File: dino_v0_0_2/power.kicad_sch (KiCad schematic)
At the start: 2 parts, among them J10 PS_ON, J9 ATX-24

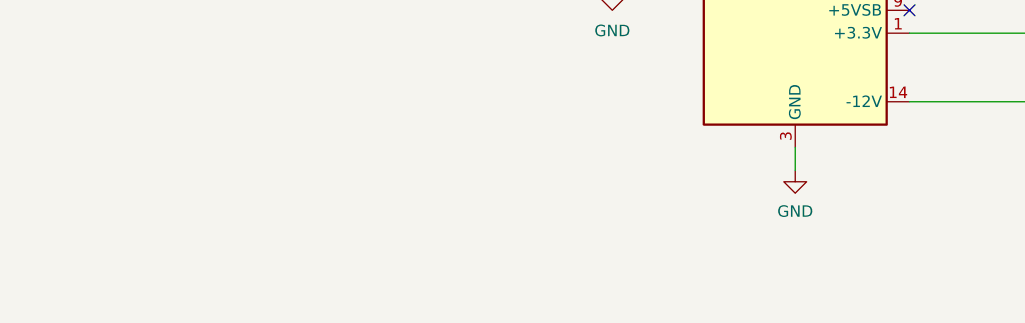
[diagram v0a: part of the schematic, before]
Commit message: feat(int): draw the interrupt block; sheet cleanup pass
New sheet dino_v0_0_2/interrupt.kicad_sch (page 15): U80-U87, R28 4.7k
pull-up on ~{IRQ}, R29 100R on the block's CLK branch, C83-C90. Every
pin per PHASE_INT SECTION 3, checked against the plan with kicad_netlist
and kicad-cli (146 pins, 0 mismatches).

Old sheets (SECTION 3.2): U28.4 lifted off GND to INJECT; U61.3 to
END_OR_ACCEPT; U36.1 to PC_UP_GATED; U49 D0-3 cut from U48 Za-Zd and
routed through U87 as FLAG_NEXT0-3 / FLAG_D0-3; FLAG_C/Z/V/N and the
five decoder outputs made global. dino_serial: U104 74LS05, INTR ->
~{IRQ}, C4.

Placement pass on every sheet: bus entries and global labels no longer
share wires; M, CW, T, IRB and SA buses kept as labelled keys. Nets
diffed against HEAD per sheet: only the intended changes and a rotated
C29. Project ERC: 0 errors. MODULE CONTRACT stamps regenerated.

Co-Authored-By: Claude Fable 5.1 <noreply@anthropic.com>
Claude-Session: https://claude.ai/code/session_01JGxSS4MVUcaZdKZGtKroSg
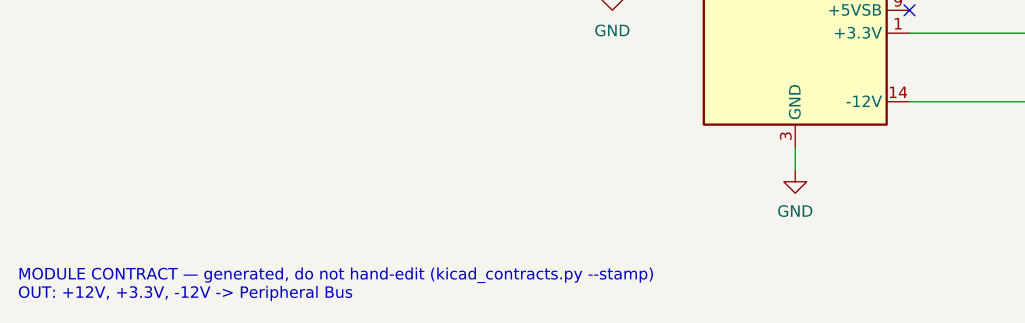
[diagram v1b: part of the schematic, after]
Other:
- note added: "MODULE CONTRACT — generated, do not hand-edit (kicad_contracts.py --stamp) OUT: +12V, +3.3V, -12V -> Peripheral Bus"
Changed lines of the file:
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@@
 		(comment 4 "A Turing-Complete 8-bit \"Computer\"")
+	)
+	(text "MODULE CONTRACT — generated, do not hand-edit (kicad_contracts.py --stamp)\nOUT: +12V, +3.3V, -12V -> Peripheral Bus"
+		(exclude_from_sim no)
+		(at 15.24 121.25 0)
+		(effects
+			(font
+				(size 1.27 1.27)
+			)
+			(justify left bottom)
+		)
 	)
 	(text "POWER IS OFF THE SHELF: picoPSU-160-XT or picoPSU-120-WI-25 in J9.\nRails drawn are what the unit delivers: +5V, +3.3V, +12V, -12V, GND.\nNo -5V exists on any 24-pin ATX unit since 2003; none is drawn.\n-12V is 50-100mA for the WHOLE machine (unit dependent): every card\nstates its +/-12V draw on its root page.\nPS_ON#: the unit runs while J10 is shorted. Panel switch or jumper.\n+5VSB and PWR_OK: real pins, nothing consumes them."

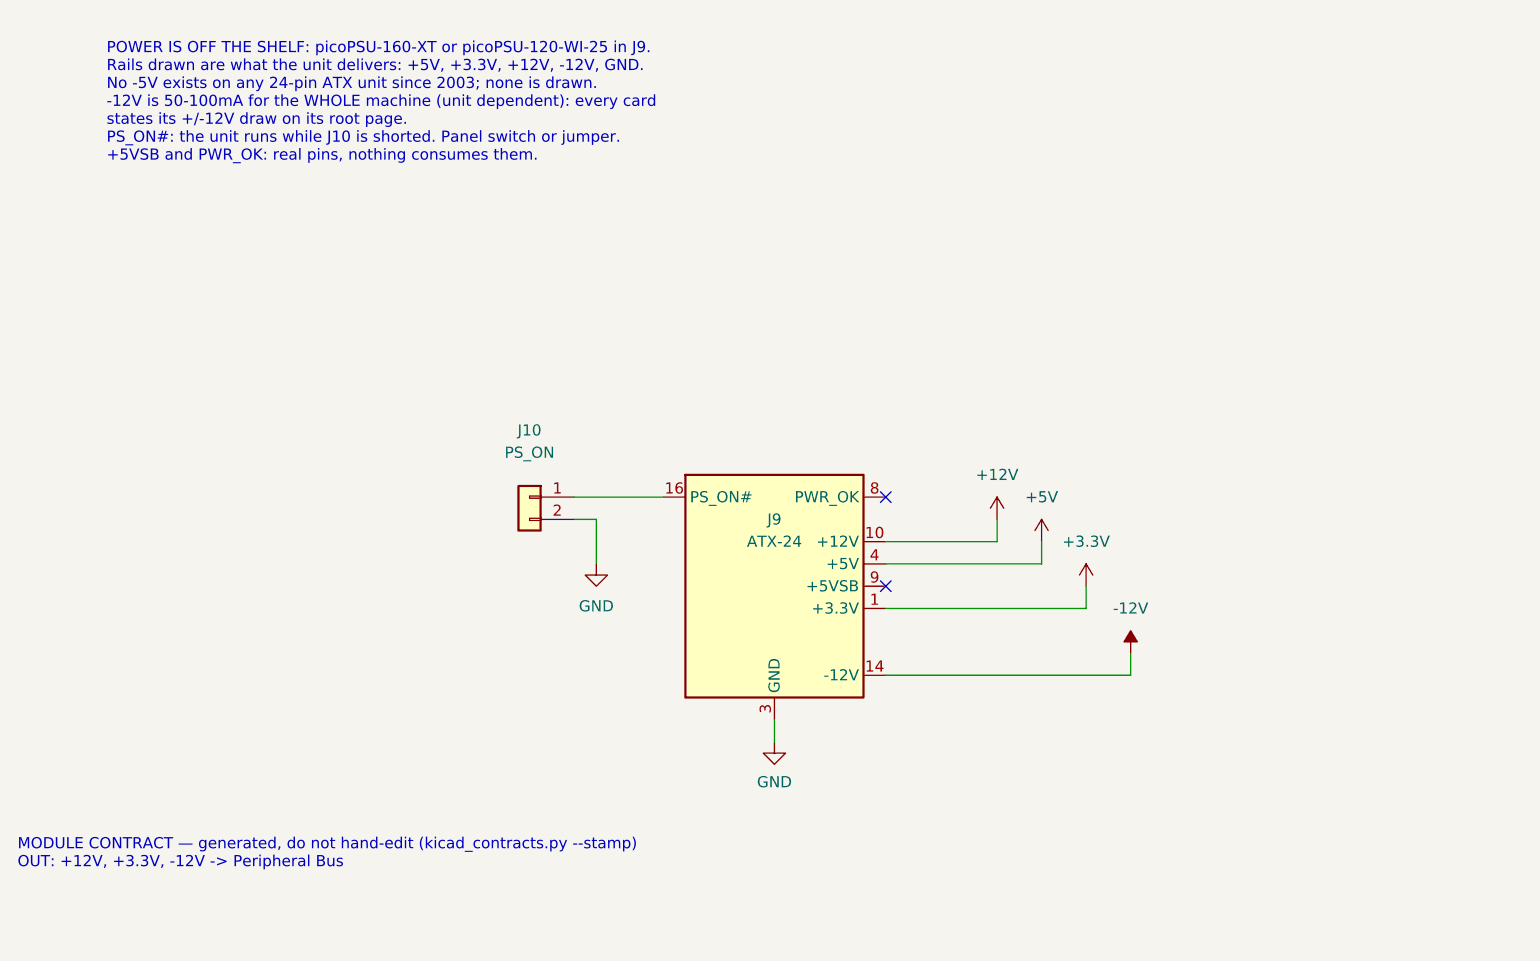
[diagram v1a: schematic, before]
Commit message: feat(pcb): sync board to schematic; fuse, bulk caps, RDY pull-up
Update PCB from schematic: the INT block (U80-U87), U76, the four
copper fixes (WR_GATE, CLK_ALU, INJECT, PC_UP gate) and the renumbered
W pull-ups (R9-R13, R30-R32 replace R4-R8, R25-R27). DRC schematic
parity 0.

Power: an old ATX tower supply into J9. +5V enters through F1 (3A
slow-blow, 5x20), J9's 5V pins on +5V_IN; C91 470uF + C92 10uF bulk;
PWR_FLAG on +5V. R33 10k pull-up on RDY. ERC unchanged from the
2026-10-06 baseline. Fix duplicate #PWR158 on the interrupt sheet.

Co-Authored-By: Claude Opus 5.5 <noreply@anthropic.com>
Claude-Session: https://claude.ai/code/session_01JGxSS4MVUcaZdKZGtKroSg
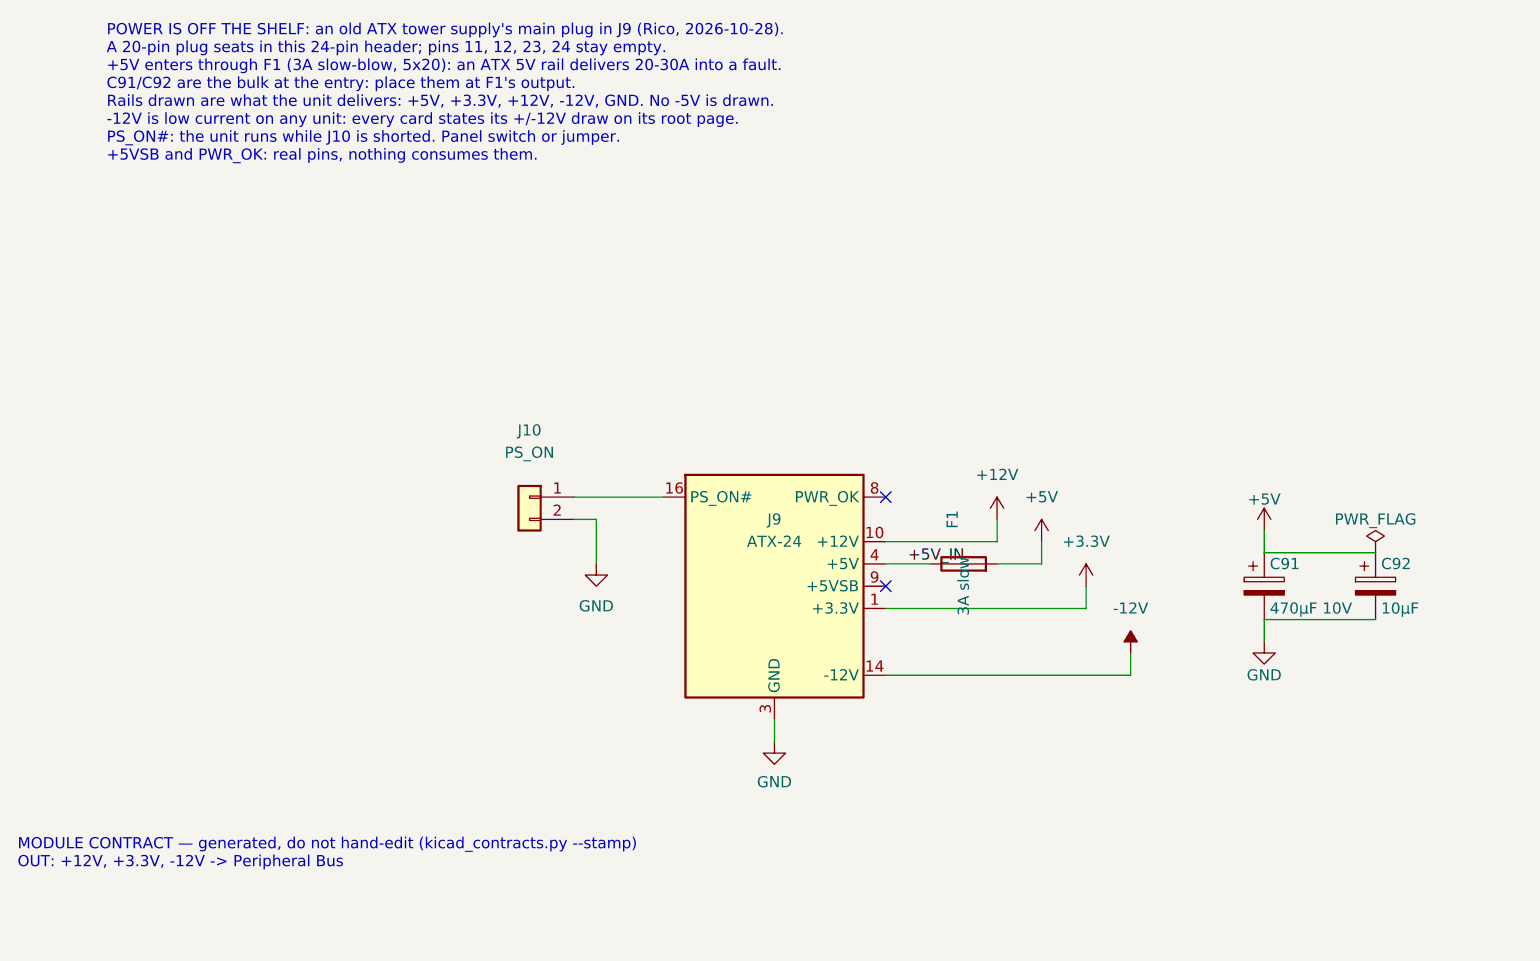
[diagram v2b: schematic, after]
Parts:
- added C91: 470µF 10V, Capacitor_THT:CP_Radial_D8.0mm_P3.50mm, symbol Device:C_Polarized
- added C92: 10µF, Capacitor_THT:CP_Radial_D5.0mm_P2.00mm, symbol Device:C_Polarized
- added F1: 3A slow, Fuse:Fuseholder_Cylinder-5x20mm_Schurter_0031_8201_Horizontal_Open, symbol Device:Fuse
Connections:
- net +5V: now also C91.1, C92.1, F1.2; no longer J9.21 (+5V), J9.22 (+5V), J9.23 (+5V), J9.4 (+5V), J9.6 (+5V)
- net GND: now also C91.2, C92.2
- new net +5V_IN: F1.1, J9.21 (+5V), J9.22 (+5V), J9.23 (+5V), J9.4 (+5V), J9.6 (+5V)
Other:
- note added: "POWER IS OFF THE SHELF: an old ATX tower supply's main plug in J9 (Rico, 2026-10-28). A 20-pin plug seats in this 24-pin header; pins 11, 12, 23, 24 stay empty. +5V enters through F1 (3A slow-blow, 5x20): an ATX 5V rail delivers 20-30A into a fault. C91/C92 are the bulk at the entry: place them at F1's output. Rails drawn are what the unit delivers: +5V, +3.3V, +12V, -12V, GND. No -5V is drawn. -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"
- note removed: "POWER IS OFF THE SHELF: picoPSU-160-XT or picoPSU-120-WI-25 in J9. Rails drawn are what the unit delivers: +5V, +3.3V, +12V, -12V, GND. No -5V exists on any 24-pin ATX unit since 2003; none is drawn. -12V is 50-100mA for the WHOLE machine (unit dependent): every card states its +/-12V draw on its root page. PS_ON#: the unit runs while J10 is shorted. Panel switch or jumper. +5VSB and PWR_OK: real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"

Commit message: feat(pcb): five grounded M3 mounting holes
H1-H5 (MountingHole_3.2mm_M3_Pad_Via, pad + stitching vias to the GND
plane) on the power sheet, pin 1 on GND. H1-H4 at the corners, 5 mm in
(H3 shifted to x 8.81 to clear J11); H5 at (85.88, 217.96), an interior
spot no track or part crosses, so the routing from 32aaa36 is unchanged.
KiCad DRC: 0 unconnected, 0 errors, 0 warnings, schematic parity 0.
ERC unchanged from the 2026-10-06 baseline.

Co-Authored-By: Claude Opus 5.5 <noreply@anthropic.com>
Claude-Session: https://claude.ai/code/session_01JGxSS4MVUcaZdKZGtKroSg
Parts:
- added H1, H2, H3, H4, H5: M3 GND, MountingHole:MountingHole_3.2mm_M3_Pad_Via, symbol Mechanical:MountingHole_Pad
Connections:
- net GND: now also H1.1, H2.1, H3.1, H4.1, H5.1

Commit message: feat(pcb): Rev 1.0 pre-order batch, debug access, no fuse
From the five-way pre-order review:

- Debug: J14 clock select at U27.3 (1.024 MHz / 512k / 256k / 128k /
  STEP), STEP debounced from SW3 through the spare U56 5->6 Schmitt;
  J15 LA header (16 control signals, a GND beside each); J16 power for
  the OB LEDs; DNP cap pads C94/C95/C96 on CLK at U6.2, CLK_ALU at
  U47.11 and CW15 (HALT) at U61.5; 15 GND scope loops so every IC but
  two is within 50 mm of one, plus a +5V test point.
- Power: F1 removed, no fuse (Rico); J9's +5V solid to the plane;
  bulk C97-C100 100 uF spread across the board; C92 ceramic.
- Layout: U6 beside U27 (its CLK pin was 138 mm out on raw CLK), C1/R1
  beside U56, RST_SIG in RESET and CLK_R / CLK_INT / CLK_M / CLK_SEL in
  CLK, thermal gap 0.3 mm (GND plane slots from 25 mm to under 8 mm),
  tracks >= 0.2 mm with no neckdown (6/6 mil tier), board min track rule.
- Values to match the bench: U56 SN7414N, U36 74LS00, U51 DM7400N,
  Y1 4.096 MHz.
- Edge socket: silk outline and a pin-1 arrow (unkeyed; a reversed card
  shorts +5V).

Re-routed by Freerouting 2.5.0 from an empty board. KiCad DRC 0
unconnected / 0 errors, schematic parity 0, one text_thickness warning
on the TrueType board text; ERC at its 74 baseline; test_pcb_envelope
7/7. Clock copper: CLK 296 mm, ~{CLK} 283, CLK_B 162, CLK_ALU 48.
Fab: fabrication/dino_rev_1_0_gerbers_20261029_1153.zip.

Co-Authored-By: Claude Opus 5.5 <noreply@anthropic.com>
Claude-Session: https://claude.ai/code/session_01JGxSS4MVUcaZdKZGtKroSg
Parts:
- removed F1: 3A slow, Fuse:Fuseholder_Cylinder-5x20mm_Schurter_0031_8201_Horizontal_Open, symbol Device:Fuse
- C92: value 10µF -> 10µF ceramic; footprint Capacitor_THT:CP_Radial_D5.0mm_P2.00mm -> Capacitor_THT:C_Disc_D5.0mm_W2.5mm_P2.50mm
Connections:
- net +5V_IN is gone; now on net +5V: J9.21 (+5V), J9.22 (+5V), J9.23 (+5V), J9.4 (+5V), J9.6 (+5V)
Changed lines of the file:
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@@
+		)
+	)
+	(wire
+		(pts
+			(xy 119.38 86.36)
+			(xy 127 86.36)
 		)
 	)
@@
 		)
 	)
-	(label "+5V_IN"
-		(at 116.84 86.36 0)
-		(effects
-			(font
-				(size 1.27 1.27)
-			)
-			(justify left bottom)
-		)
-	)
 	(symbol
 		(lib_id "Connector:ATX-24")
@@
 	)
 	(symbol
-		(lib_id "Device:Fuse")
-		(at 123.19 86.36 90)
-		(unit 1)
-		(in_bom yes)
-		(on_board yes)
-		(dnp no)
-		(property "Reference" "F1"
-			(at 121.92 81.28 0)
-			(effects
-				(font
-					(size 1.27 1.27)
-				)
-			)
-		)
-		(property "Value" "3A slow"
-			(at 123.19 88.9 0)
-			(effects
-				(font
-					(size 1.27 1.27)
-				)
-			)
-		)
-		(property "Footprint" "Fuse:Fuseholder_Cylinder-5x20mm_Schurter_0031_8201_Horizontal_Open"
-			(at 123.19 86.36 0)
-			(hide yes)
-			(effects
-				(font
-					(size 1.27 1.27)
-				)
-			)
-		)
-		(property "Datasheet" ""
-			(at 123.19 86.36 0)
-			(hide yes)
-			(effects
-				(font
-					(size 1.27 1.27)
-				)
-			)
-		)
-		(property "Description" "Fuse"
-			(at 123.19 86.36 0)
-			(hide yes)
-			(effects
-				(font
-					(size 1.27 1.27)
-				)
-			)
-		)
-		(instances
-			(project "dino_v0_0_2"
-				(path "/e43166a5-d972-471d-b3cf-9f4f12c7f541/10bea0ab-627a-4d28-8ace-426d08390de5"
-					(reference "F1")
-					(unit 1)
-				)
-			)
-		)
-	)
-	(symbol
 		(lib_id "Device:C_Polarized")
 		(at 157.48 88.9 0)
@@
 			)
 		)
-		(property "Value" "10µF"
+		(property "Value" "10µF ceramic"
 			(at 170.815 91.44 0)
 			(effects
@@
 			)
 		)
-		(property "Footprint" "Capacitor_THT:CP_Radial_D5.0mm_P2.00mm"
+		(property "Footprint" "Capacitor_THT:C_Disc_D5.0mm_W2.5mm_P2.50mm"
 			(at 170.18 88.9 0)
 			(hide yes)
@@
 					(unit 1)
 				)
-			)
-		)
-	)
-	(symbol
-		(lib_id "power:PWR_FLAG")
-		(at 170.18 85.09 0)
-		(unit 1)
-		(in_bom yes)
-		(on_board yes)
-		(dnp no)
-		(property "Reference" "#FLG01"
-			(at 170.18 83.185 0)
-			(hide yes)
-			(effects
-				(font
-					(size 1.27 1.27)
-				)
-			)
-		)
-		(property "Value" "PWR_FLAG"
-			(at 170.18 81.28 0)
-			(effects
-				(font
-					(size 1.27 1.27)
-				)
-			)
-		)
-		(property "Footprint" ""
-			(at 170.18 85.09 0)
-			(hide yes)
-			(effects
-				(font
-					(size 1.27 1.27)
-				)
-			)
-		)
-		(property "Datasheet" ""
-			(at 170.18 85.09 0)
-			(hide yes)
-			(effects
-				(font
-					(size 1.27 1.27)
-				)
-			)
-		)
-		(property "Description" "Special symbol for telling ERC where power comes from"
-			(at 170.18 85.09 0)
-			(hide yes)
-			(effects
-				(font
-					(size 1.27 1.27)
-				)
-			)
-		)
-		(instances
-			(project "dino_v0_0_2"
-				(path "/e43166a5-d972-471d-b3cf-9f4f12c7f541/10bea0ab-627a-4d28-8ace-426d08390de5"
-					(reference "#FLG01")
-					(unit 1)
-				)
